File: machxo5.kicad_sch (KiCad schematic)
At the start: 97 parts, among them J3001 PinHeader_2x5_P1.27mm_SMD, J3002 PinHeader_2x5_P1.27mm_SMD, J3003 PinHeader_2x5_P1.27mm_SMD, J3004 PinHeader_2x5_P1.27mm_SMD, J3005 PinHeader_2x5_P1.27mm_SMD, J3006 PinHeader_2x5_P1.27mm_SMD, J3007 PinHeader_2x5_P1.27mm_SMD, J3008 PinHeader_2x5_P1.27mm_SMD, J3009 PinHeader_2x5_P1.27mm_SMD, J3010 PinHeader_2x5_P1.27mm_SMD, J3011 PinHeader_2x5_P1.27mm_SMD, SW3001 SW_KSC441J70SHLFS_SMD, SW3002 SW_KSC441J70SHLFS_SMD, SW3004 SW_KSC441J70SHLFS_SMD, U3001 LFMXO5-25-7BBG400C, Y3001 Resonator_32.768kHz_ECX-31B

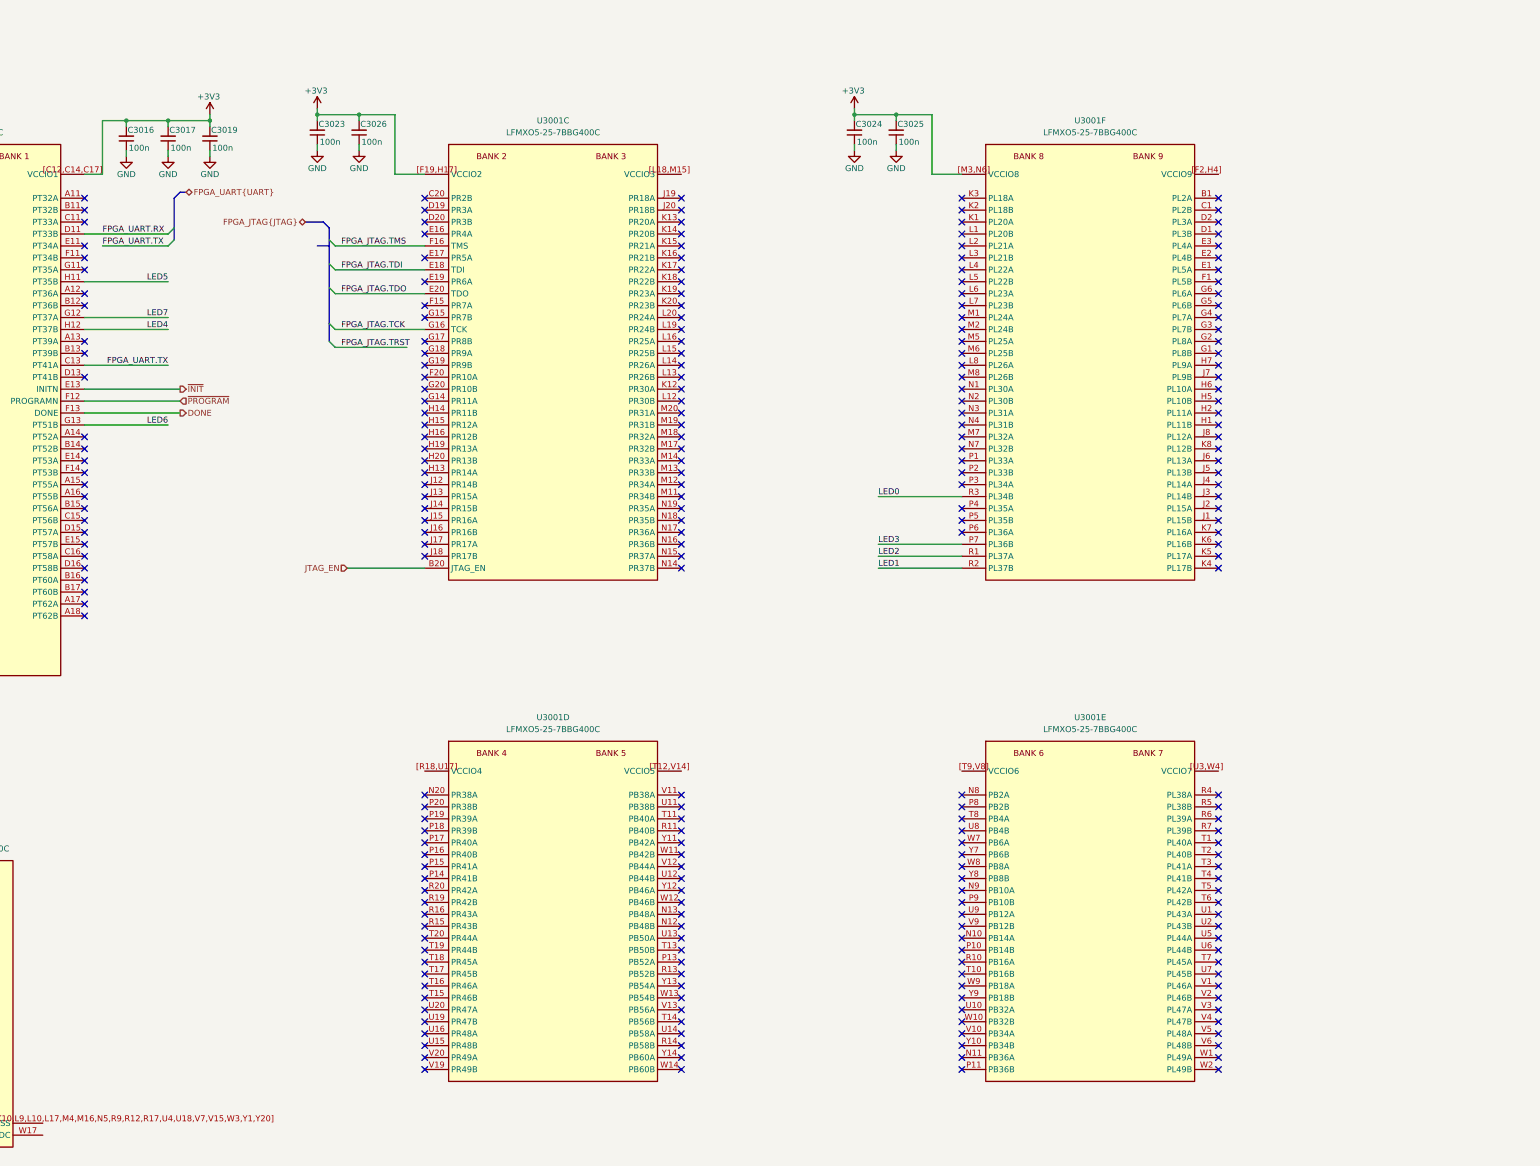
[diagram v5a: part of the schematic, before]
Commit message: [#103910] machxo5: connect 125MHz clock
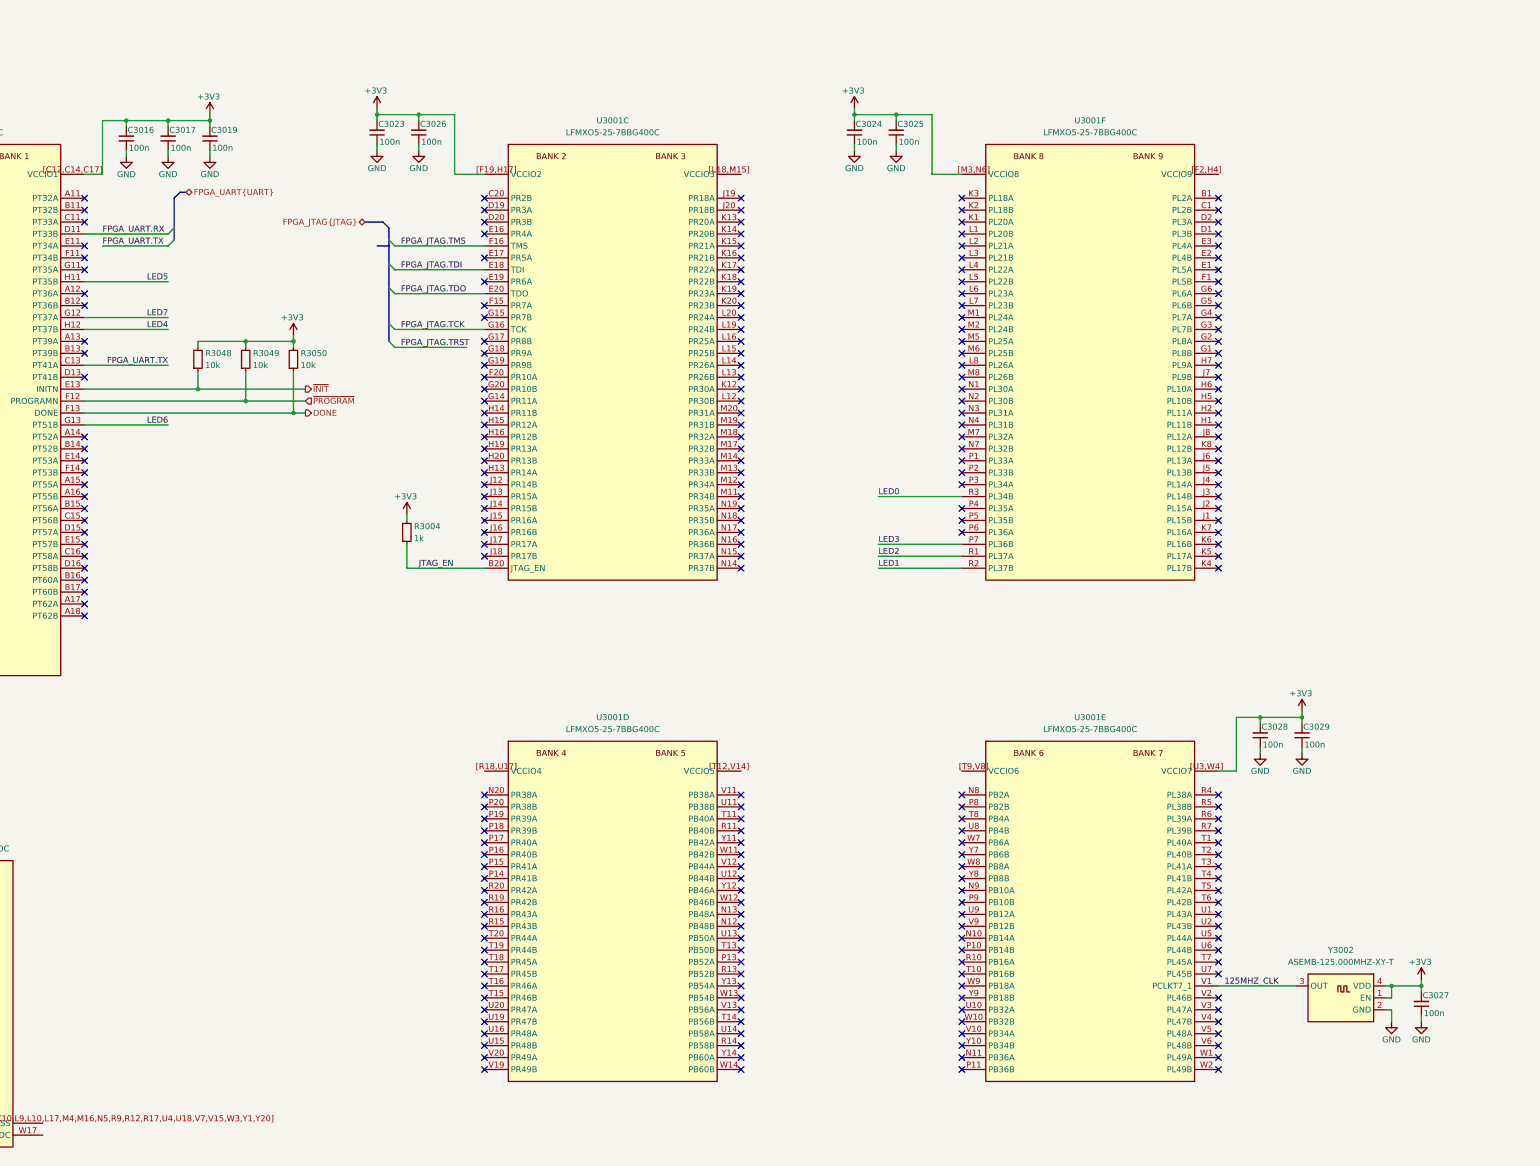
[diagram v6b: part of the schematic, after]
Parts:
- added C3027, C3028, C3029: C_100n_0402, antmicro-footprints:C_0402_1005Metric, symbol antmicroCapacitors0402:C_100n_0402
- added R3004: R_1k_0402, antmicro-footprints:R_0402_1005Metric, symbol antmicroResistors0402:R_1k_0402
- added R3048, R3049, R3050: R_10k_0402, antmicro-footprints:R_0402_1005Metric, symbol antmicroResistors0402:R_10k_0402
- added Y3002: Oscillator_125MHz_ASEMB, antmicro-footprints:Oscillator_SMD_Abracon_ASEMB_3.2x2.5mm, symbol antmicroOscillators:Oscillator_125MHz_ASEMB
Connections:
- net +3V3: now also U3001.[U3,W4] (VCCIO7), C3027.2, C3028.2, C3029.2, R3004.2, R3048.2, R3049.2, R3050.2, Y3002.1 (EN), Y3002.4 (VDD)
- net DONE: now also R3050.1
- net GND: now also C3027.1, C3028.1, C3029.1, Y3002.2 (GND)
- net JTAG_EN: now also R3004.1
- net ~{INIT}: now also R3048.1
- net ~{PROGRAM}: now also R3049.1
- net 125MHZ_CLK: now reaches U3001.V1 (PL46A/PCLKT7_1)
- net 125MHZ_CLK: now also Y3002.3 (OUT)
- no-connect marks 278 -> 277
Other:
- moved on the sheet: C3023, C3026, U3001C, U3001D

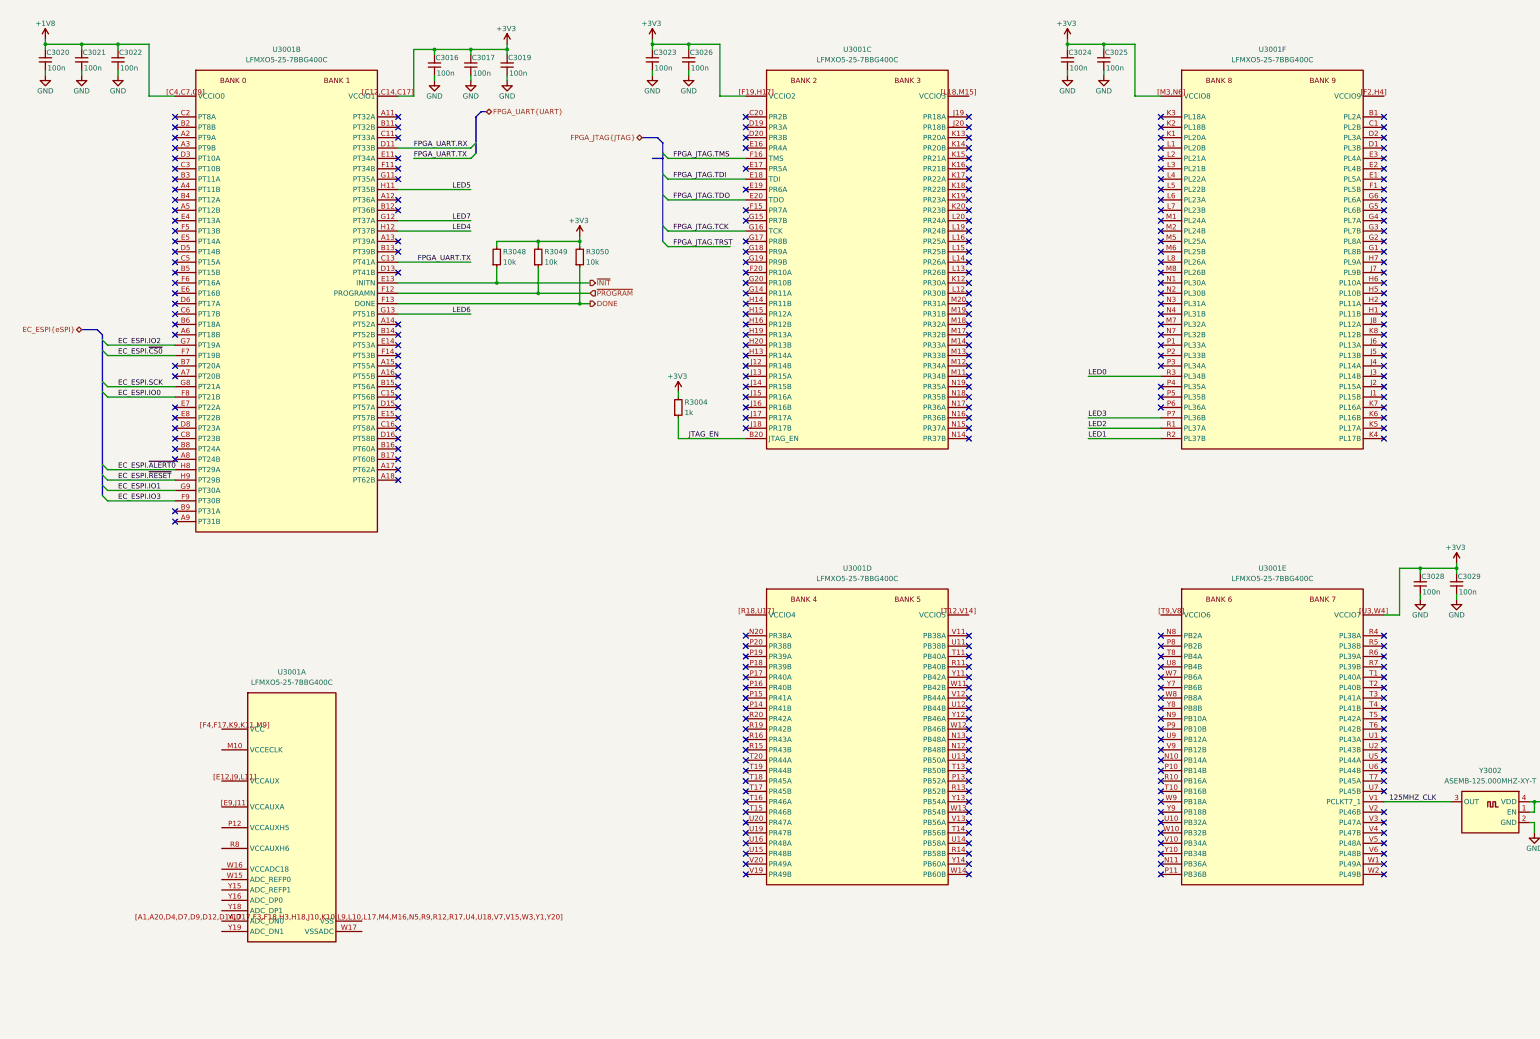
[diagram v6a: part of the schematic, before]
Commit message: [#103910] machxo5: connect power to FPGA core
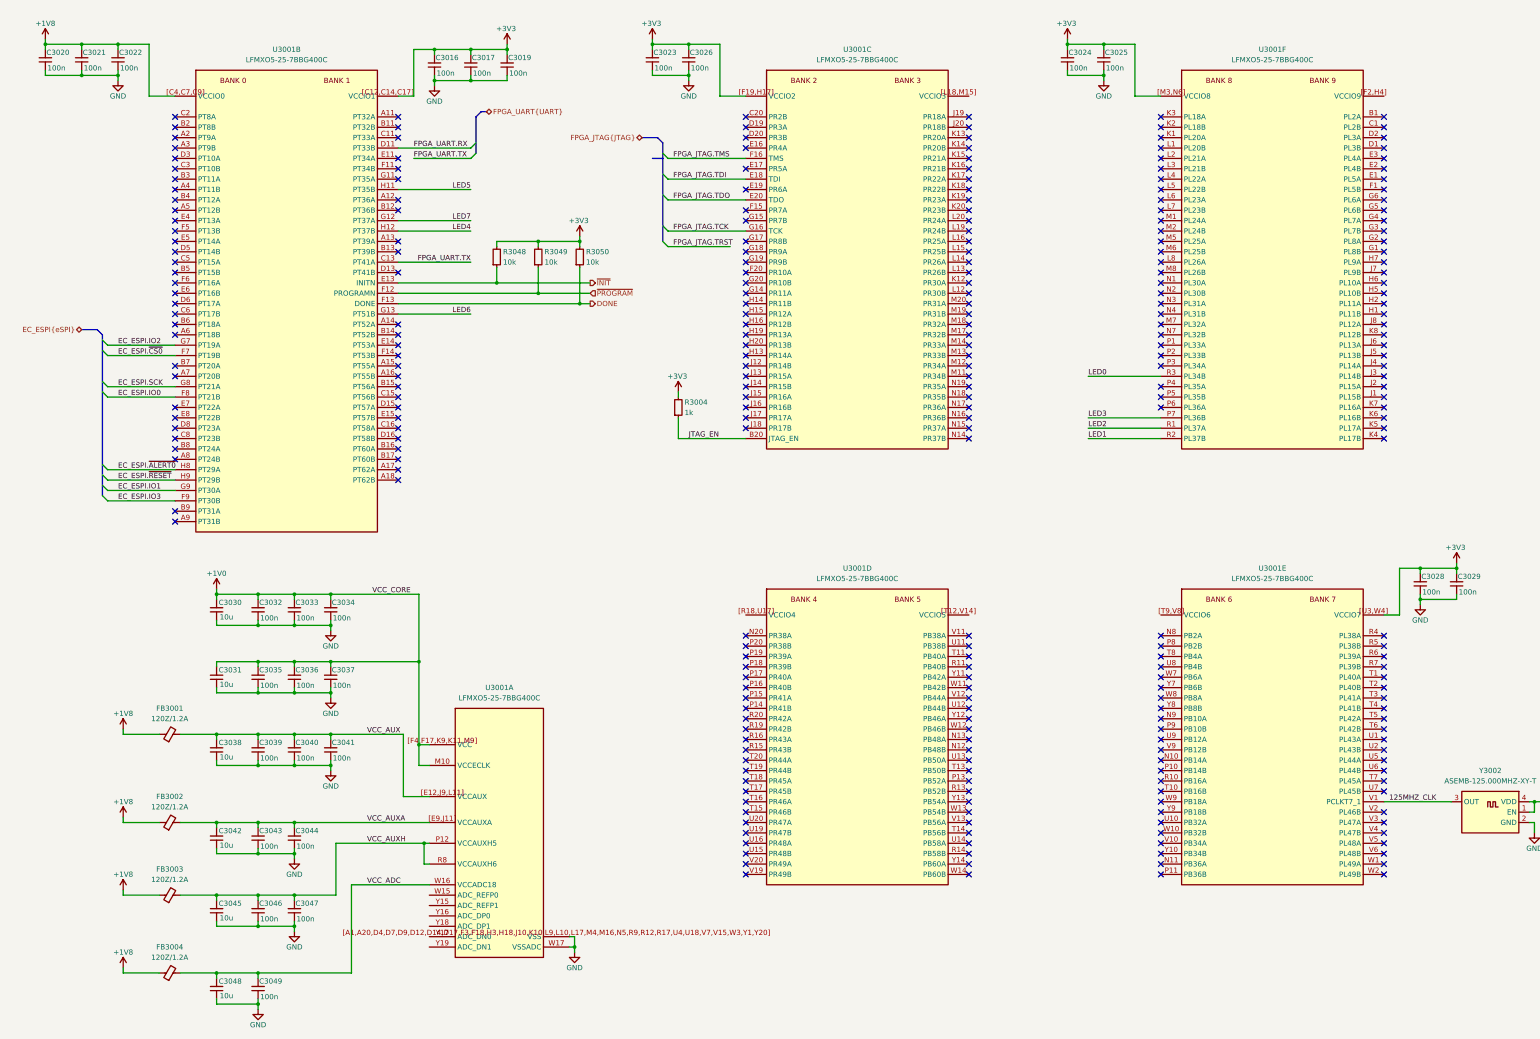
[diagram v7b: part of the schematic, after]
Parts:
- added C3030, C3031, C3038, C3042, C3045, C3048: C_10u_6.3V_0402, antmicro-footprints:C_0402_1005Metric, symbol antmicroCapacitors0402:C_10u_6.3V_0402
- added C3032, C3033, C3034, C3035, C3036, C3037, C3039, C3040, C3041, C3043, C3044, C3046, C3047, C3049: C_100n_0402, antmicro-footprints:C_0402_1005Metric, symbol antmicroCapacitors0402:C_100n_0402
- added FB3001, FB3002, FB3003, FB3004: FB_120Z_1.2A_TDK-MPZ_0402, antmicro-footprints:FB_0402_1005Metric, symbol antmicroFerriteBeadsandChips:FB_120Z_1.2A_TDK-MPZ_0402
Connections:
- net +1V8: now also FB3001.1, FB3002.1, FB3003.1, FB3004.1
- net GND: now also U3001.W17 (VSSADC), U3001.[A1,A20,D4,D7,D9,D12,D14,D17,F3,F18,H3,H18,J10,K10,L9,L10,L17,M4,M16,N5,R9,R12,R17,U4,U18,V7,V15,W3,Y1,Y20] (VSS), C3030.1, C3031.1, C3032.1, C3033.1, C3034.1, C3035.1, C3036.1, C3037.1, C3038.1, C3039.1, C3040.1, C3041.1, C3042.1, C3043.1, C3044.1, C3045.1, C3046.1, C3047.1, C3048.1, C3049.1
- net +1V0: now reaches U3001.M10 (VCCECLK)
- net +1V0: now also U3001.[F4,F17,K9,K11,M9] (VCC), C3030.2, C3031.2, C3032.2, C3033.2, C3034.2, C3035.2, C3036.2, C3037.2
- net VCC_AUXH: now reaches U3001.P12 (VCCAUXH5)
- net VCC_AUXH: now also U3001.R8 (VCCAUXH6), C3045.2, C3046.2, C3047.2, FB3003.2
- net VCC_ADC: now reaches U3001.W16 (VCCADC18)
- net VCC_ADC: now also C3048.2, C3049.2, FB3004.2
- net VCC_AUX: now reaches U3001.[E12,J9,L11] (VCCAUX)
- net VCC_AUX: now also C3038.2, C3039.2, C3040.2, C3041.2, FB3001.2
- net VCC_AUXA: now reaches U3001.[E9,J11] (VCCAUXA)
- net VCC_AUXA: now also C3042.2, C3043.2, C3044.2, FB3002.2
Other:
- moved on the sheet: U3001A

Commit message: [#103910] machxo5: connect 7-segment high digit
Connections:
- net 7SEG_H.A: now also U3001.F14 (PT53B)
- net 7SEG_H.B: now also U3001.G11 (PT35A)
- net 7SEG_H.C: now also U3001.E15 (PT57B)
- net 7SEG_H.D: now also U3001.F11 (PT34B)
- net 7SEG_H.DP: now also U3001.A18 (PT62B)
- net 7SEG_H.E: now also U3001.A15 (PT55A)
- net 7SEG_H.F: now also U3001.A16 (PT55B)
- net 7SEG_H.G: now also U3001.A17 (PT62A)
- no-connect marks 277 -> 269
